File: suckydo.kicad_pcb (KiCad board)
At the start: 2 copper layers, 76 parts, among them IC1 AP33771CFBZ-13-FA01, IC2 TS391SN2T1G, IC3 TPS561201DDCR, J1 HFW14R-1STE1H1LF, J2 USB4105-GF-A, Q1 PJA3404A, Q2 MMBT2222A, Q3 PJA3404A, Q5 MMBT2222A, Q6 PJA3404A, U1 ESP32-C6-MINI-1-H4

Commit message: layout
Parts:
- added REF**: MountingHole_3.2mm_M3, MountingHole:MountingHole_3.2mm_M3, F.Cu at (49.5, 111.8)
- added REF**: MountingHole_3.2mm_M3, MountingHole:MountingHole_3.2mm_M3, F.Cu at (99.1, 111.8)
- added REF**: MountingHole_3.2mm_M3, MountingHole:MountingHole_3.2mm_M3, F.Cu at (99.1, 163.8)
- added REF**: MountingHole_3.2mm_M3, MountingHole:MountingHole_3.2mm_M3, F.Cu at (49.5, 163.8)
- Pedal1: value Screw_Terminal_01x02 -> Pedal
- Pump1: value Screw_Terminal_01x02 -> Pump
- R19, R7, R8: footprint Resistor_SMD:R_0402_1005Metric -> Resistor_SMD:R_0805_2012Metric
- Valve1: value Screw_Terminal_01x02 -> Valve
- moved J1 118.7 mm to (56.1, 153.2)
- moved C18 112.2 mm to (63.7, 139.7)
- moved L2 111.9 mm to (71.9, 136.8), turned to 90 degrees
- moved D2 107.7 mm to (53.4, 124.2), turned to -90 degrees
- moved C4 103.2 mm to (57.5, 123.8), turned to 90 degrees
- moved C2 102.8 mm to (81.6, 154.4), turned to 90 degrees
- moved C8 102.3 mm to (64.3, 124.3), turned to -90 degrees
- moved C9 102.0 mm to (62.2, 120.9), turned to 90 degrees
- moved C1 101.0 mm to (87.4, 154.4), turned to -90 degrees
- moved R8 100.1 mm to (67.3, 110.0), turned to -90 degrees
- moved C3 99.3 mm to (83.5, 154.4), turned to 90 degrees
- moved C6 97.8 mm to (67.3, 113.4), turned to -90 degrees
- moved C11 97.1 mm to (65.5, 118.1), turned to 180 degrees
- moved C7 97.0 mm to (70.8, 122.8), turned to -90 degrees
- moved R19 96.2 mm to (73.7, 128.6)
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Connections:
- J1 pad 10: /ESP_STATUS3 -> /ESP_STATUS2
- J1 pad 11: /ESP_STATUS4 -> /ESP_STATUS1
- J1 pad 12: /ESP_IO6 -> /ESP_IO20
- J1 pad 13: /ESP_IO7 -> /ESP_IO21
- J1 pad 2: /DISPLAY_SDA -> /DISPLAY_SCL
- J1 pad 4: /DISPLAY_SCL -> /DISPLAY_SDA
- J1 pad 8: /ESP_STATUS1 -> /ESP_STATUS4
- J1 pad 9: /ESP_STATUS2 -> /ESP_STATUS3
- U1 pad 15: /ESP_IO6 -> unconnected-(U1-IO6-Pad15)
- U1 pad 16: /ESP_IO7 -> unconnected-(U1-IO7-Pad16)
- U1 pad 19: /ESP_STATUS1 -> unconnected-(U1-IO14-Pad19)
- U1 pad 20: /ESP_STATUS2 -> /PEDAL_IN
- U1 pad 24: unconnected-(U1-IO18-Pad24) -> /DISPLAY_SCL
- U1 pad 25: /ESP_STATUS3 -> /DISPLAY_SDA
- U1 pad 26: /ESP_STATUS4 -> /ESP_IO20
- U1 pad 27: /DISPLAY_SCL -> /ESP_IO21
- U1 pad 28: /DISPLAY_SDA -> /ESP_STATUS1
- U1 pad 29: unconnected-(U1-IO23-Pad29) -> /ESP_STATUS2
- U1 pad 30: unconnected-(U1-RXD0-Pad30) -> /ESP_STATUS3
- U1 pad 31: unconnected-(U1-TXD0-Pad31) -> /ESP_STATUS4
- U1 pad 5: /PEDAL_IN -> unconnected-(U1-IO2-Pad5)
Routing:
- net /D+: track 0.00 -> 41.1 mm, vias 0 -> 2
- net /ESP_RESET: track 0.00 -> 40.2 mm, vias 0 -> 4
- net Net-(Q2-B): track 0.00 -> 39.7 mm, vias 0 -> 2
- net /D-: track 0.00 -> 38.9 mm, vias 0 -> 2
- net +12V: track 0.00 -> 35.6 mm, vias 0 -> 18
- net /PEDAL_IN: track 0.00 -> 35.3 mm, vias 0 -> 2
- net +5V: track 0.00 -> 34.3 mm, vias 0 -> 2
- net +3.3V: track 0.00 -> 26.4 mm, vias 0 -> 19
- net /ESP_BOOT: track 0.00 -> 24.5 mm, vias 0 -> 2
- net /DISPLAY_SCL: track 0.00 -> 22.2 mm
- net /ESP_STATUS4: track 0.00 -> 20.5 mm
- net /ESP_STATUS3: track 0.00 -> 19.1 mm
- net /DISPLAY_SDA: track 0.00 -> 17.8 mm
- net /ESP_STATUS2: track 0.00 -> 17.8 mm
- net /12V_EN: track 0.00 -> 17.1 mm, vias 0 -> 2
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- added copper zone on F.Cu, net +12V
- added copper zone on In2.Cu, net +12V
- added copper zone on F.Cu, net +3.3V
- added copper zone on In2.Cu, net +3.3V
- added copper zone on F.Cu, net /PUMP_LO
- added copper zone on In2.Cu, net /PUMP_LO
- added copper zone on F.Cu, net /VALVE_LO
- added copper zone on In2.Cu, net /VALVE_LO
- added copper zone on B.Cu, net GND
- added copper zone on F.Cu, net GND
- added copper zone on In1.Cu, net GND
- added copper zone on In2.Cu, net GND
- added copper zone on F.Cu, net Net-(IC1-VCC)
- added copper zone on F.Cu, net Net-(IC3-SW)
- added copper zone on In2.Cu, net Net-(IC3-SW)
- added copper zone on F.Cu, net Net-(IC3-VBST)
- added copper zone on F.Cu, net Net-(PS1-SW)
- added copper zone on F.Cu, net VBUS
- added copper zone on In2.Cu, net VBUS
- added copper zone on B.Cu, net VBUS_SW
- added copper zone on F.Cu, net VBUS_SW
- added copper zone on In1.Cu, net VBUS_SW
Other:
- board outline added: 59.9 x 61.5 mm
- copper layers 2 -> 4
- board text added: "+"
- board text added: "JLCJLCJLCJLC"
- board text added: "suckyDO"

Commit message: drc fixes
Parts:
- removed the REF** at (99.1, 111.8)
- removed the REF** at (99.1, 163.8)
- removed the REF** at (49.5, 163.8)
- added REF**: MountingHole_3.2mm_M3, MountingHole:MountingHole_3.2mm_M3, F.Cu at (98.4, 111.8)
- added REF**: MountingHole_3.2mm_M3, MountingHole:MountingHole_3.2mm_M3, F.Cu at (98.4, 162.6)
- added REF**: MountingHole_3.2mm_M3, MountingHole:MountingHole_3.2mm_M3, F.Cu at (49.5, 162.6)
- moved Pump1 2.59 mm to (95.8, 141.2), turned to 90 degrees
- moved Valve1 2.51 mm to (95.9, 120.5), turned to 90 degrees
- moved R12 0.64 mm to (76.3, 118.0)
- moved R11 0.58 mm to (70.7, 118.0)
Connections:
- J1 pad MP1: GND -> unconnected-(J1-PadMP1)
- J1 pad MP2: GND -> unconnected-(J1-PadMP2)
- Pump1 pad 1: +12V -> /PUMP_LO
- Pump1 pad 2: /PUMP_LO -> +12V
- Valve1 pad 1: +12V -> /VALVE_LO
- Valve1 pad 2: /VALVE_LO -> +12V
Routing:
- net /CC1: track 16.2 -> 17.4 mm, vias 2 -> 3
- net /CC2: track 16.1 -> 17.3 mm, vias 2 -> 3
- net Net-(IC1-DP): track 4.07 -> 3.39 mm
- net Net-(IC1-DN): track 5.79 -> 5.13 mm
- net VBUS_SW: vias 22 -> 21
- net Net-(IC1-VCC): vias 8 -> 6
- net GND: vias 57 -> 68
- net +3.3V: vias 19 -> 16

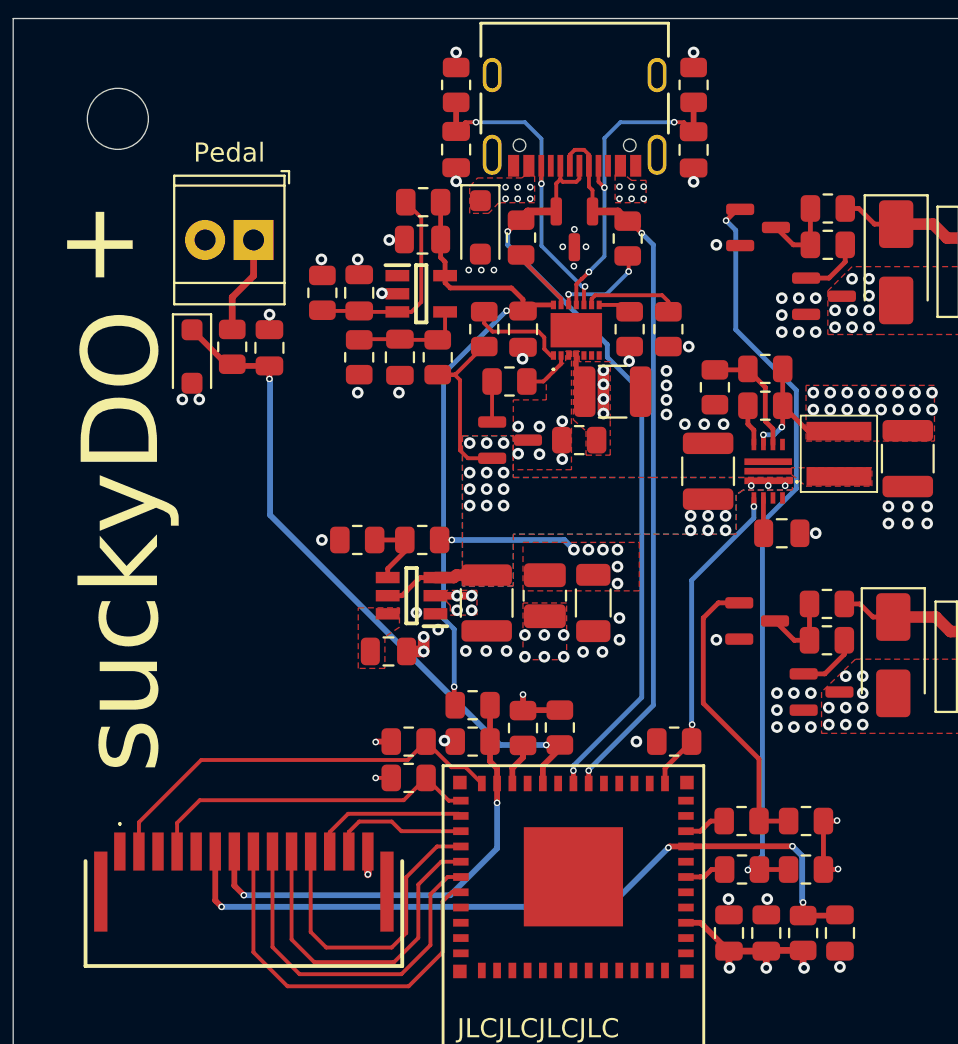
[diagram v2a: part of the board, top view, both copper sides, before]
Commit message: drill size fixes
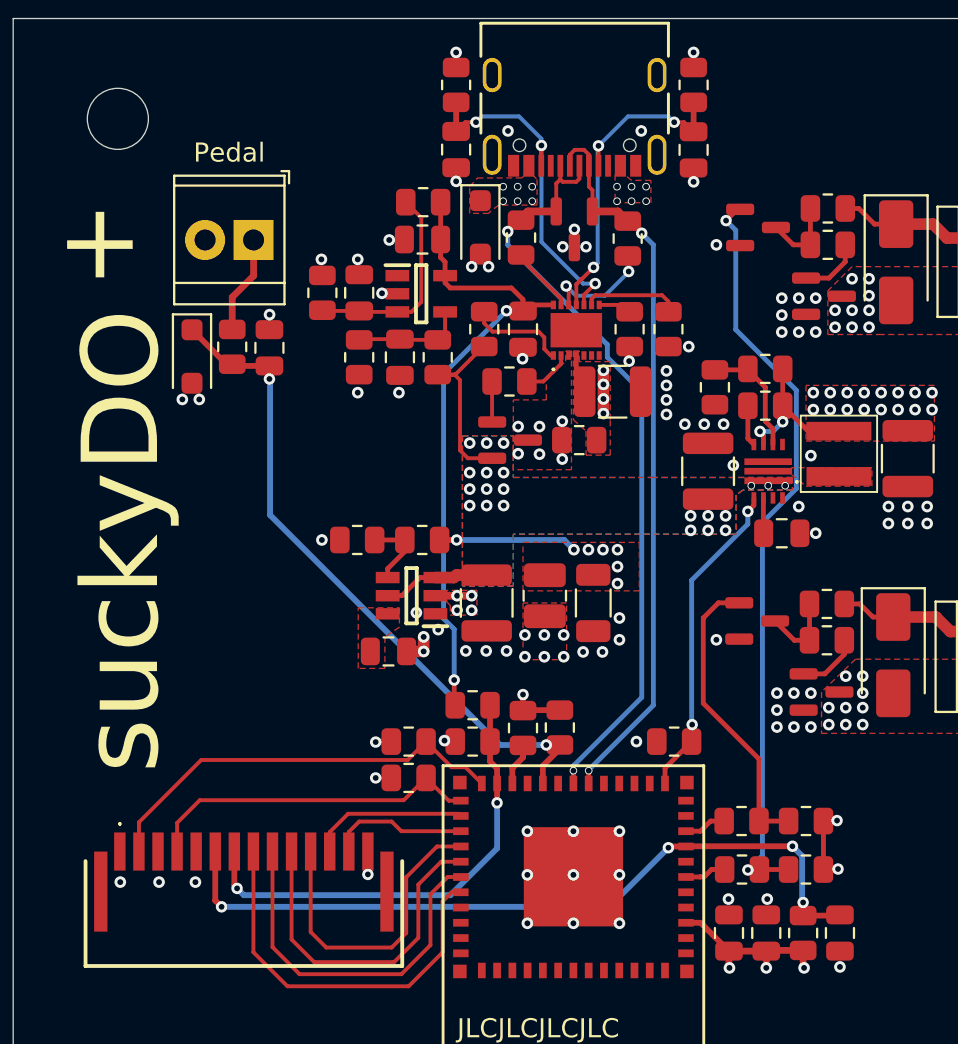
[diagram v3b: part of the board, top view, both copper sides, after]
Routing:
- net /CC2: track 17.3 -> 18.4 mm
- net Net-(IC1-DN): track 5.13 -> 5.99 mm
- net GND: vias 68 -> 83
